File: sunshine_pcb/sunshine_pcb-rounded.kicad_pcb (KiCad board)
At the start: 4 copper layers, 45.5 x 66.7 mm, 54 parts, among them J1 PWRIN, J2 Conn_01x04, J3 PWROUT, J5 VerticalUSB, Q1 AO3400A, SW1 SW_SPST, U1 ESP32-S3-WROOM-1, U2 SPX1117M3, U3 LIS3MDL, U4 ADXL375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

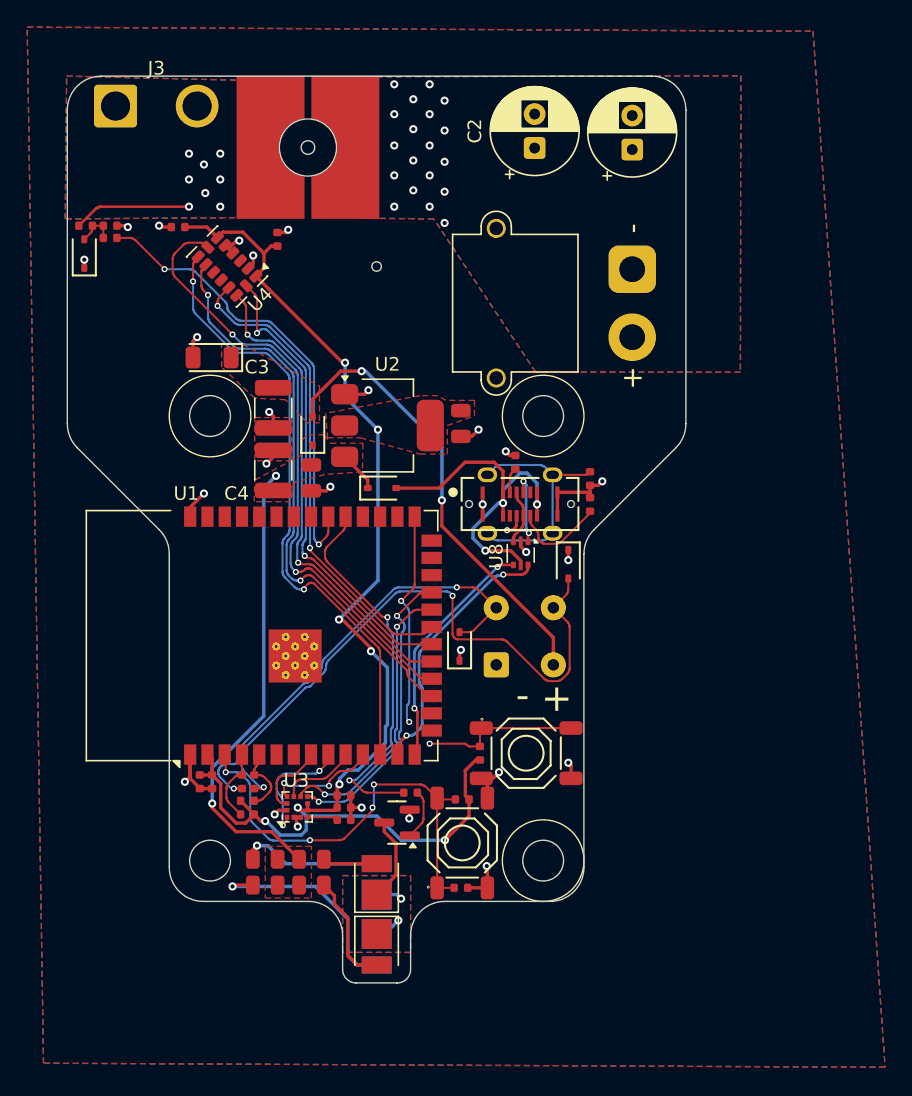
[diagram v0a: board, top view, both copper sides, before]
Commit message: Fix the extension, round the other tracks
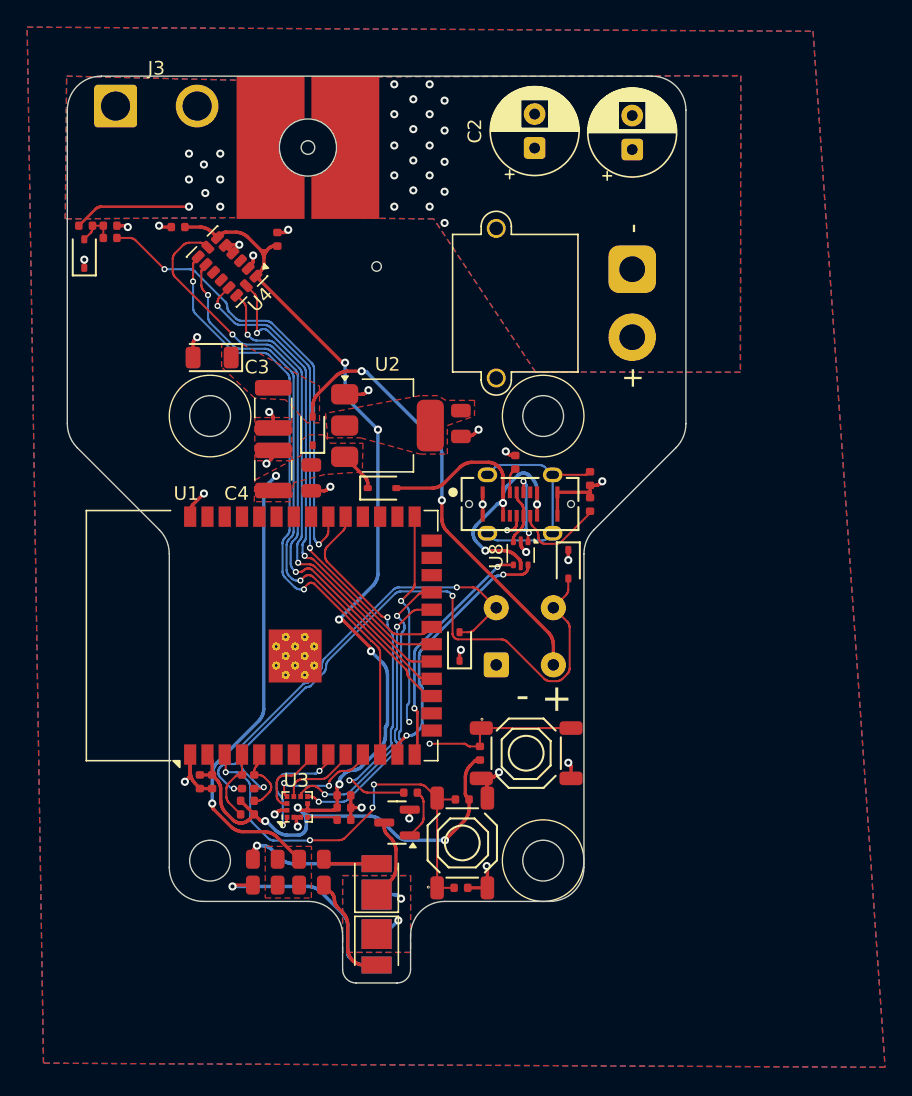
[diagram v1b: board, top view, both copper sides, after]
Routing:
- net +3V3: track 96.0 -> 97.1 mm
- net VBUS: track 28.0 -> 27.5 mm

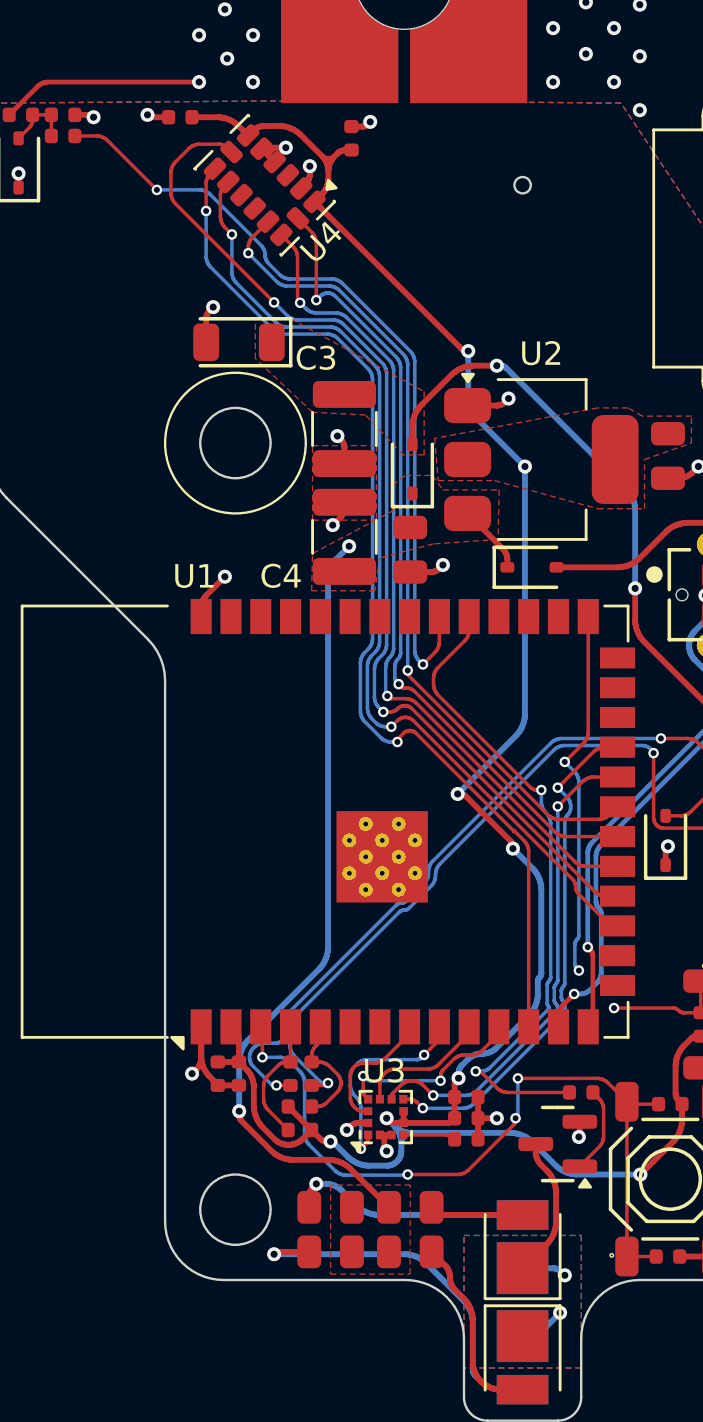
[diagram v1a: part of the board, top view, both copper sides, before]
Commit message: Fix hole clearance
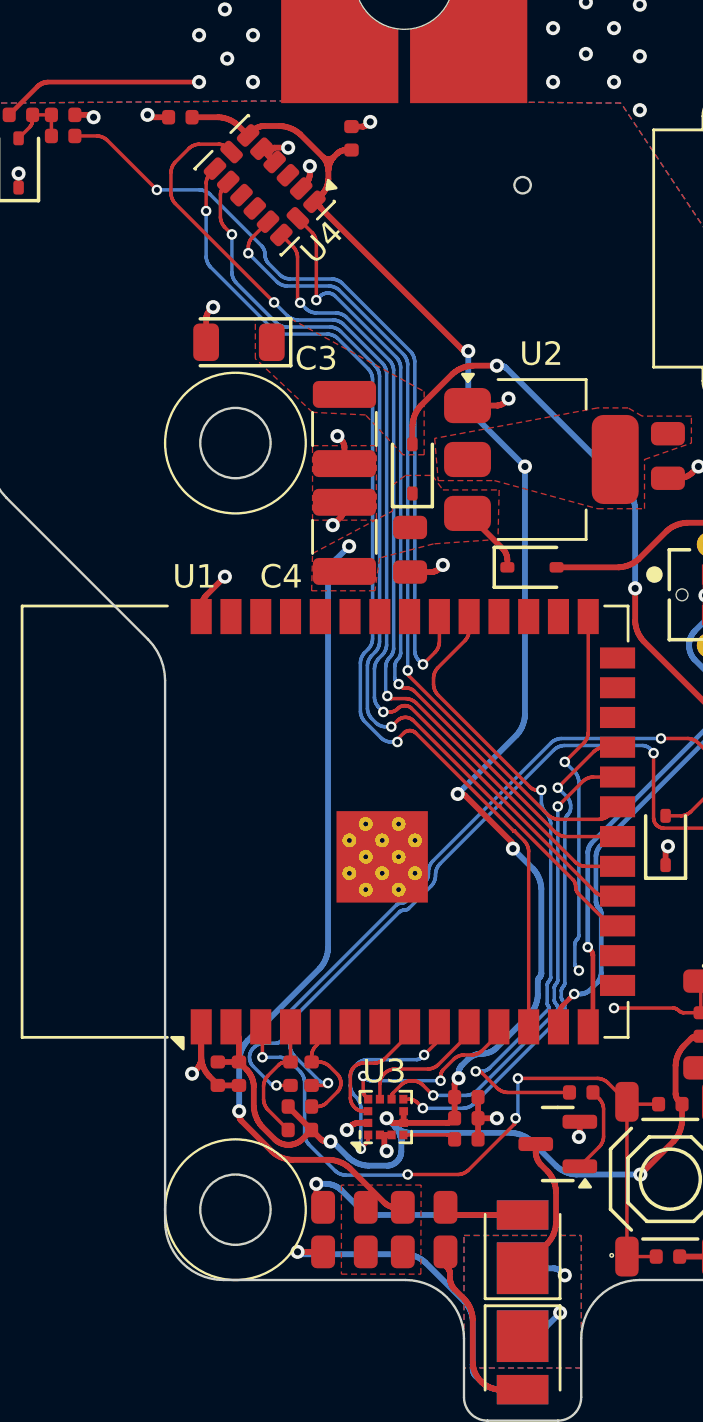
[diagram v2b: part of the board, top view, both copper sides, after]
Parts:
- moved R10 0.59 mm to (92.4, 143.6)
- moved R12 0.59 mm to (92.4, 145.5)
- moved R16 0.59 mm to (95.8, 143.6)
- moved R8 0.59 mm to (95.8, 145.5)
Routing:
- net Net-(D5-A): track 15.9 -> 14.5 mm
- net Net-(D4-A): track 10.4 -> 10.9 mm
- net +5V: track 37.0 -> 37.5 mm

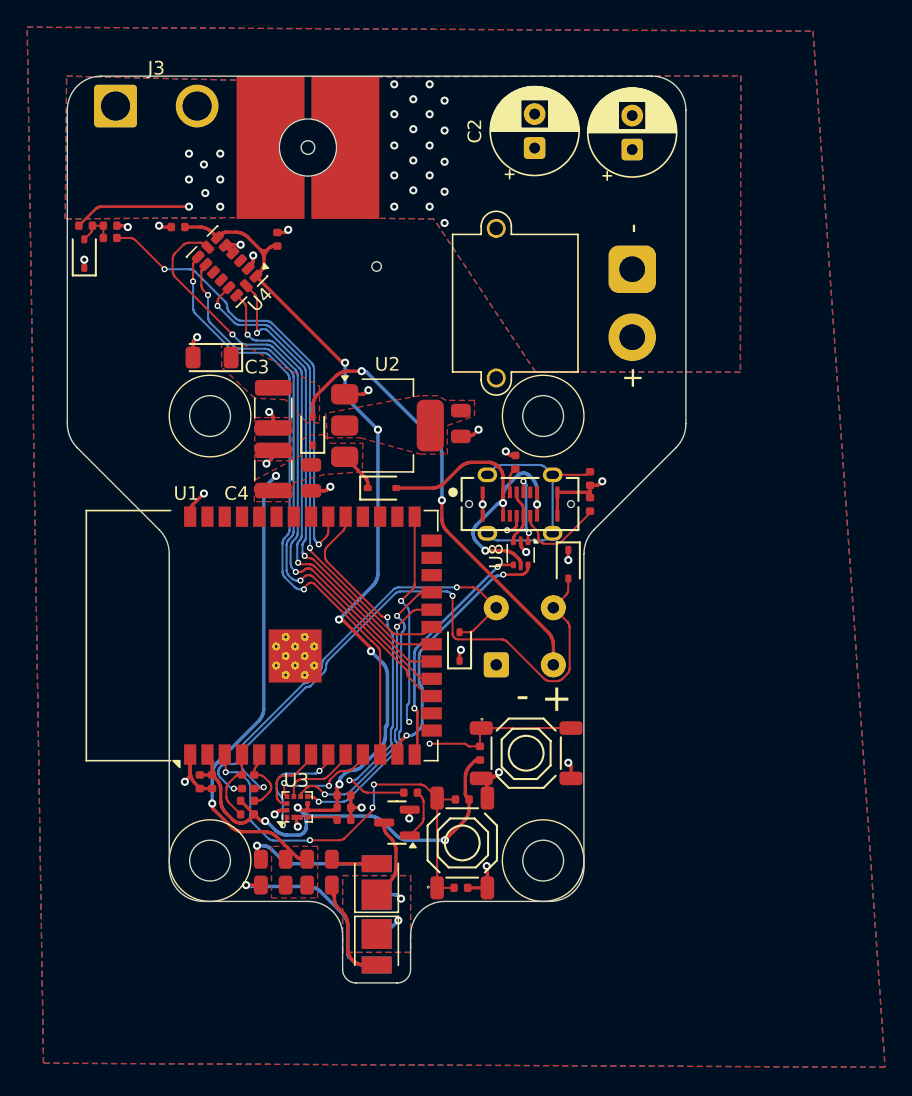
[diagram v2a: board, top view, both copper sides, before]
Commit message: Fix VSENSE net
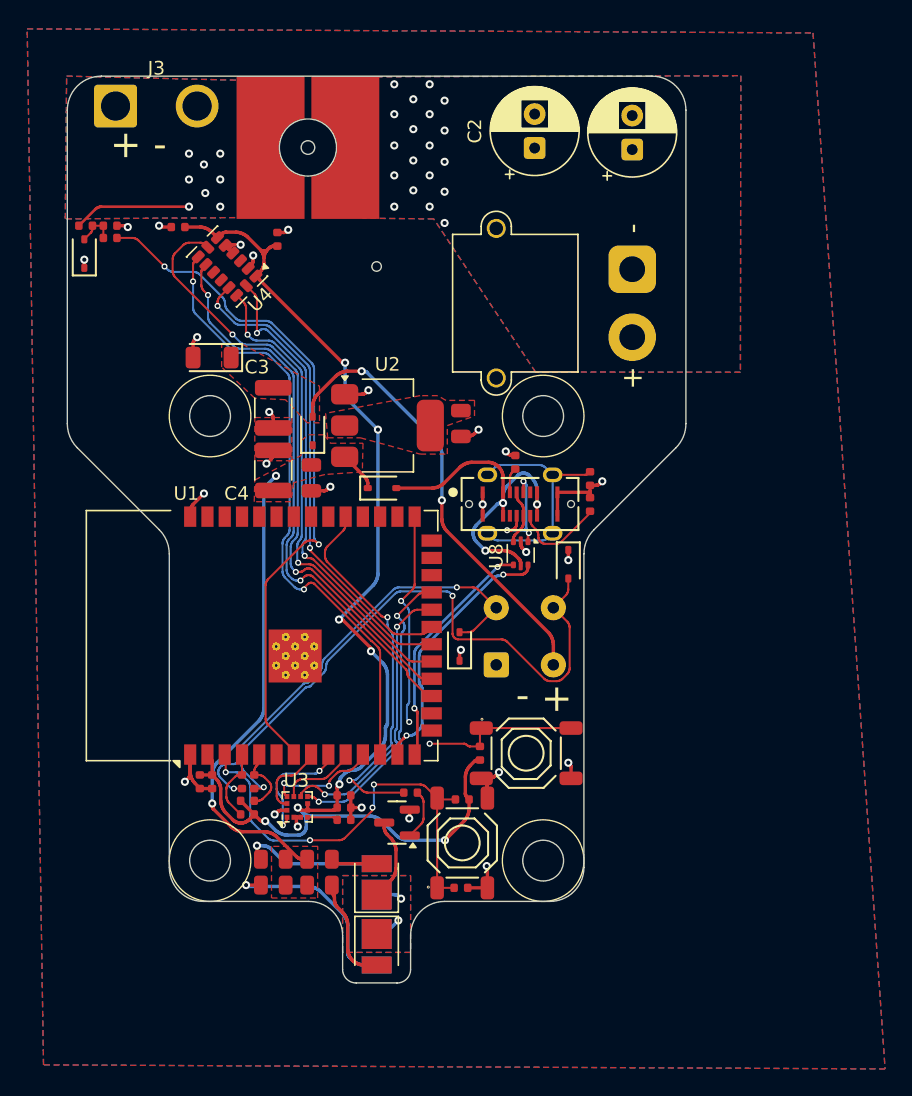
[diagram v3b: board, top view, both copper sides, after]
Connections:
- U1 pad 32: /VSENSE -> unconnected-(U1-IO39-Pad32)
- U1 pad 7: unconnected-(U1-IO7-Pad7) -> /VSENSE
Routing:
- net /VSENSE: track 34.0 -> 50.5 mm
